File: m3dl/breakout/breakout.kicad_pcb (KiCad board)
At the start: 2 copper layers, 40 x 26 mm, 15 parts, among them J1 WEST TOP, J2 EAST TOP, J3 WEST BOT, J4 EAST BOT, J5 North, J6 South

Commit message: Final Tweaks before manufacture
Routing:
- net /PWR: track 32.0 -> 33.7 mm
- net /PYRO4: track 36.0 -> 37.2 mm
- net /PYRO1: track 25.6 -> 26.4 mm
- net /PYRO3: track 34.6 -> 35.2 mm
- net /PYRO2: track 30.1 -> 30.7 mm
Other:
- net class Default: clearance 0.2 -> 0.15
- rule trace_clearance: 0.2 -> 0.15

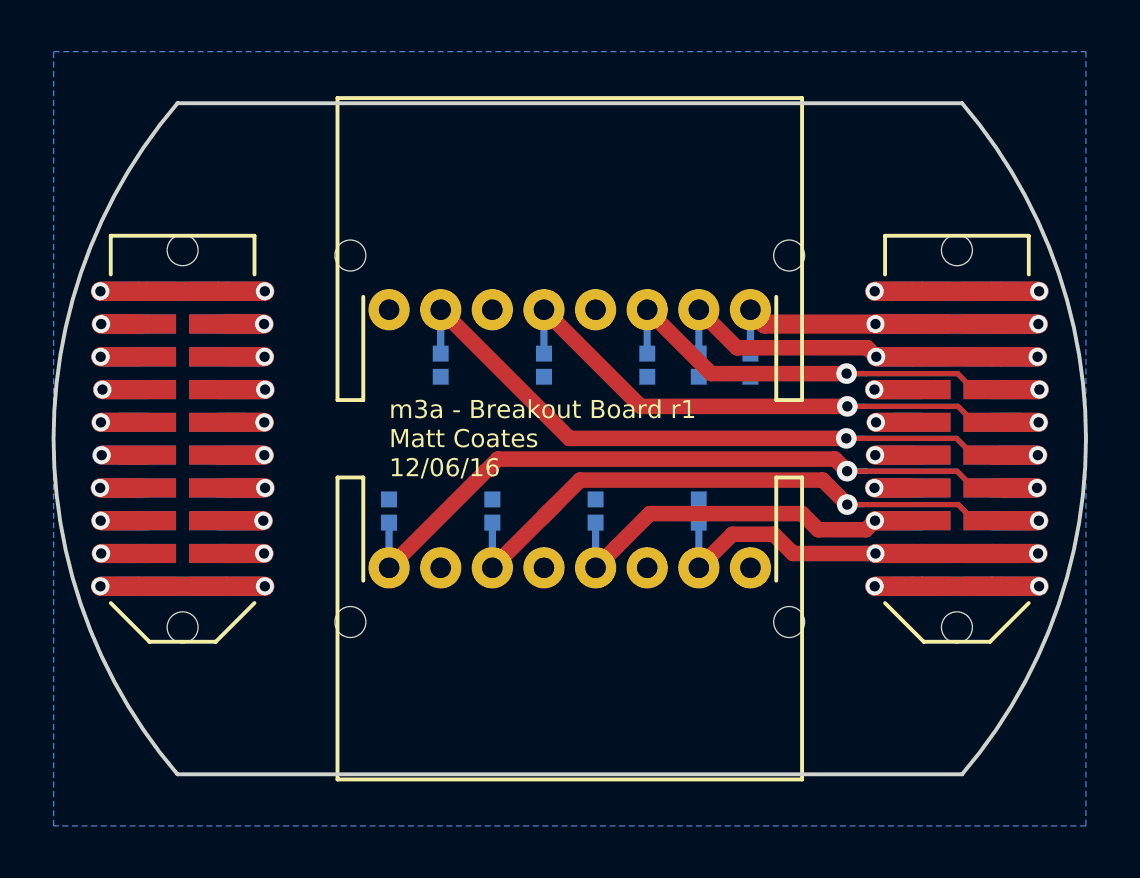
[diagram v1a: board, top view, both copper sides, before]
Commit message: Add breakout r2 schematic and pcb
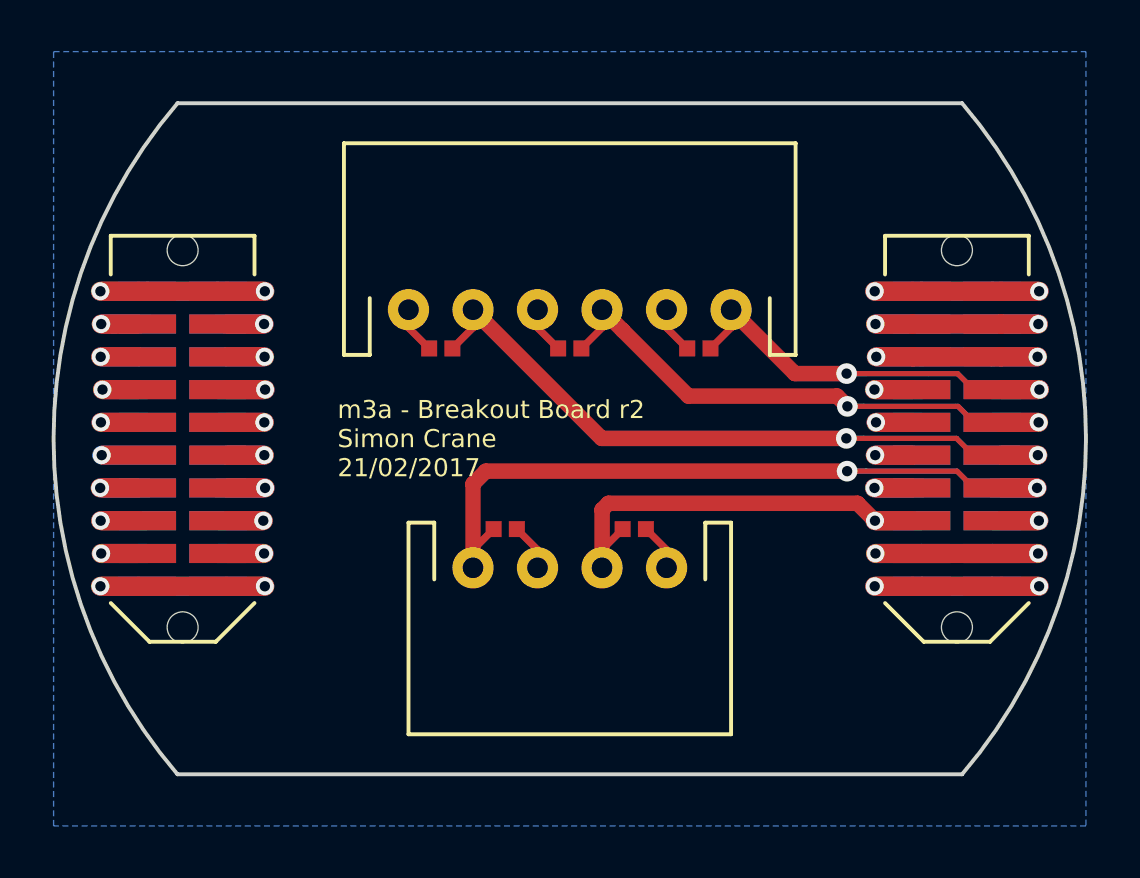
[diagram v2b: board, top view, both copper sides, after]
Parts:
- removed D6, D7, D8, D9: ESD_DIODE, agg:0402
- D1, D2, D3, D4, D5: moved to F.Cu
- J5: value North -> CONN_01x06; footprint agg:S08B-PASK-2 -> agg:S6B-EH
- J6: value South -> CONN_01x04; footprint agg:S08B-PASK-2 -> agg:S4B-EH
- moved D1 10.0 mm to (105.0, 96.5), turned to 180 degrees
- moved D3 8.03 mm to (95.0, 96.5), turned to 180 degrees
- moved D4 4.55 mm to (97.5, 103.5), turned to 0 degrees
- moved D5 2.60 mm to (102.5, 103.5), turned to 0 degrees
- moved D2 1.19 mm to (100.0, 96.5), turned to 180 degrees
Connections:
- D1 pad 1: /PYRO3 -> /PYRO1
- D3 pad 1: /PYRO1 -> /PYRO3
- D5 pad 1: /CHARGE -> /5v_CAM
- J5 pad 1: /PYRO_SO -> /PYRO1
- J5 pad 2: /PYRO_SI -> GND
- J5 pad 3: /PYRO1 -> /PYRO2
- J5 pad 5: /PYRO2 -> /PYRO3
- J6 pad 3: /PWR -> /5v_CAM
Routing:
- net /PWR: track 33.7 -> 5.00 mm, vias 2 -> 1
- net /CHARGE: track 22.0 -> 12.6 mm
- net /PYRO_SI: track 21.8 -> 12.5 mm
- net GND: track 51.0 -> 60.1 mm
- net /PYRO_SO: track 19.4 -> 12.6 mm
- net /PYRO1: track 26.4 -> 23.3 mm
- net /PYRO2: track 30.7 -> 28.6 mm
- net /PYRO4: track 37.2 -> 35.5 mm
- net /5v_CAM: track 17.3 -> 18.5 mm
- net /PYRO3: track 35.2 -> 34.1 mm
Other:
- board text added: "m3a - Breakout Board r2 Simon Crane 21/02/2017"
- board text removed: "CHG"
- board text removed: "PWR"
- board text removed: "SIN"
- board text removed: "SOUT"
- board text removed: "m3a - Breakout Board r1 Matt Coates 12/06/16"

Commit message: Update JST-EH footprints on breakout board
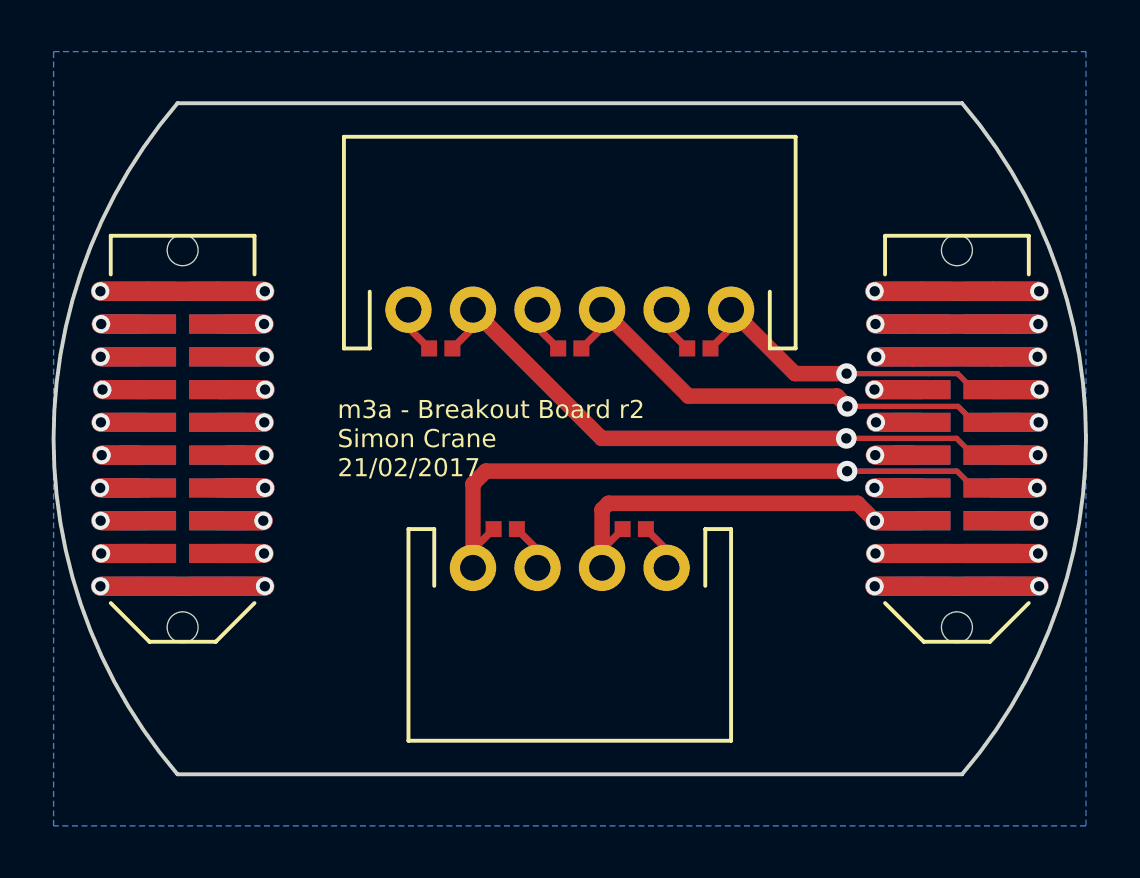
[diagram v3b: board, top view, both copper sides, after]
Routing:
- net /PWR: track 5.00 -> 3.27 mm
- net /3v3_DL: track 2.55 -> 3.19 mm

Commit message: Potential update to breakout board r2
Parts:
- added J7: PYRO2, agg:S2B-EH, F.Cu at (100.0, 95.0)
- added J8: PYRO4, agg:S2B-EH, F.Cu at (96.0, 105.0)
- added J9: 5v_CAM, agg:S2B-EH, F.Cu at (104.0, 105.0)
- J5: value CONN_01x06 -> PYRO1; footprint agg:S6B-EH -> agg:S2B-EH
- J6: value CONN_01x04 -> PYRO3; footprint agg:S4B-EH -> agg:S2B-EH
- moved J6 12.7 mm to (92.2, 95.0), turned to 0 degrees
- moved D2 7.75 mm to (92.2, 96.2)
- moved J5 7.75 mm to (107.8, 95.0)
- moved D3 5.01 mm to (100.0, 96.2)
- moved D1 2.76 mm to (107.8, 96.2)
- moved D4 1.52 mm to (96.0, 103.8)
- moved D5 1.52 mm to (104.0, 103.8)
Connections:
- D2 pad 1: /PYRO2 -> /PYRO3
- D3 pad 1: /PYRO3 -> /PYRO2
- J6 pad 1: /PYRO4 -> /PYRO3
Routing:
- net /PYRO3: track 33.7 -> 37.1 mm
- net /PYRO1: track 22.8 -> 19.9 mm
- net /5v_CAM: track 18.3 -> 15.6 mm
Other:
- board text added: "+5V_CAM-"
- board text added: "+PYRO1-"
- board text added: "+PYRO2-"
- board text added: "+PYRO3-"
- board text added: "+PYRO4-"
